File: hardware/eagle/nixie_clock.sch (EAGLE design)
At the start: 62 parts, among them IC1 74141N, IC10 7477N, IC11 74141N, IC12 7477N, IC13 74AC11238, IC2 7477N, IC3 74141N, IC4 7477N, IC5 74141N, IC6 7477N, IC7 74141N, IC8 7477N, IC9 74141N, J1_180V 22-27-2021-02, J1_5V1 22-27-2021-02, J1_5V2 22-27-2021-02

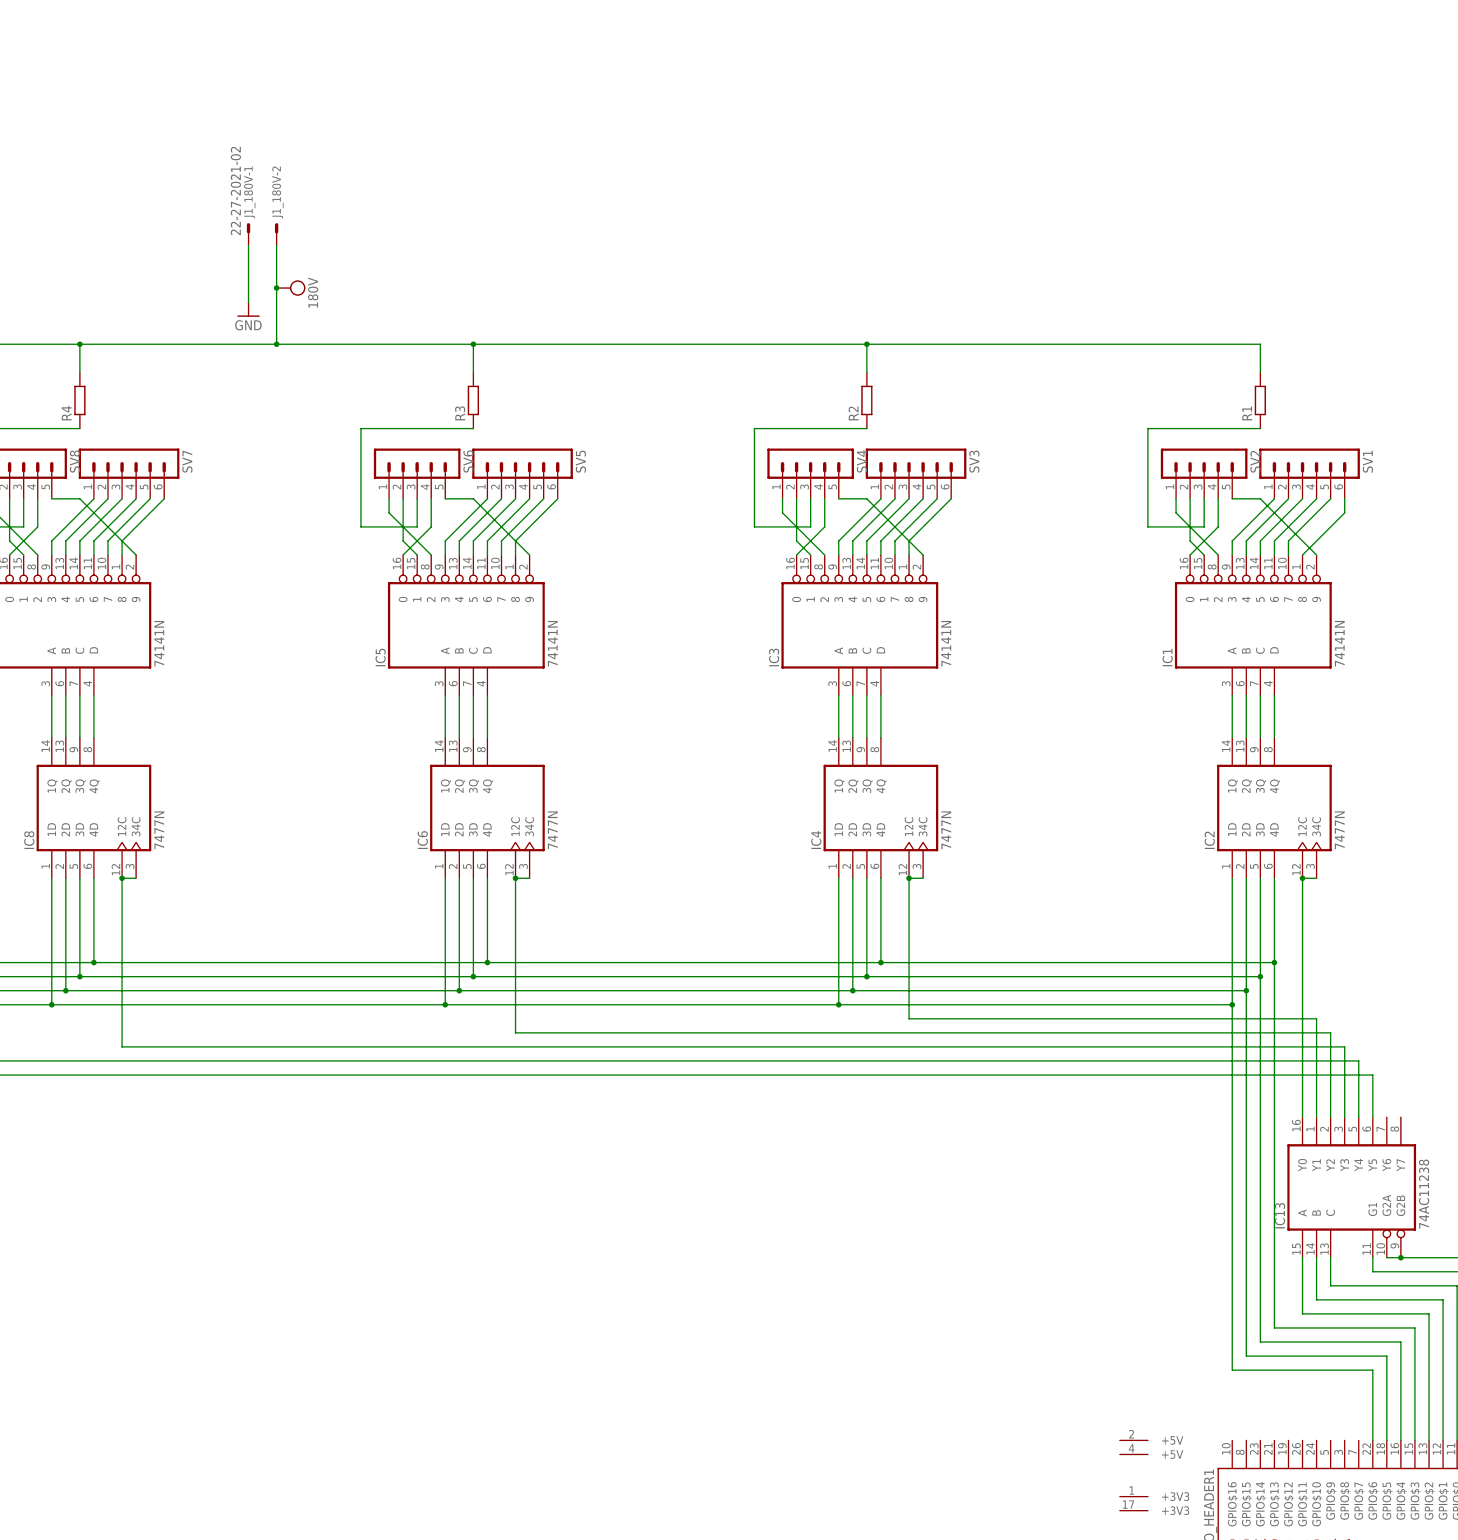
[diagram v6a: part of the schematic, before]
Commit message: Added relay
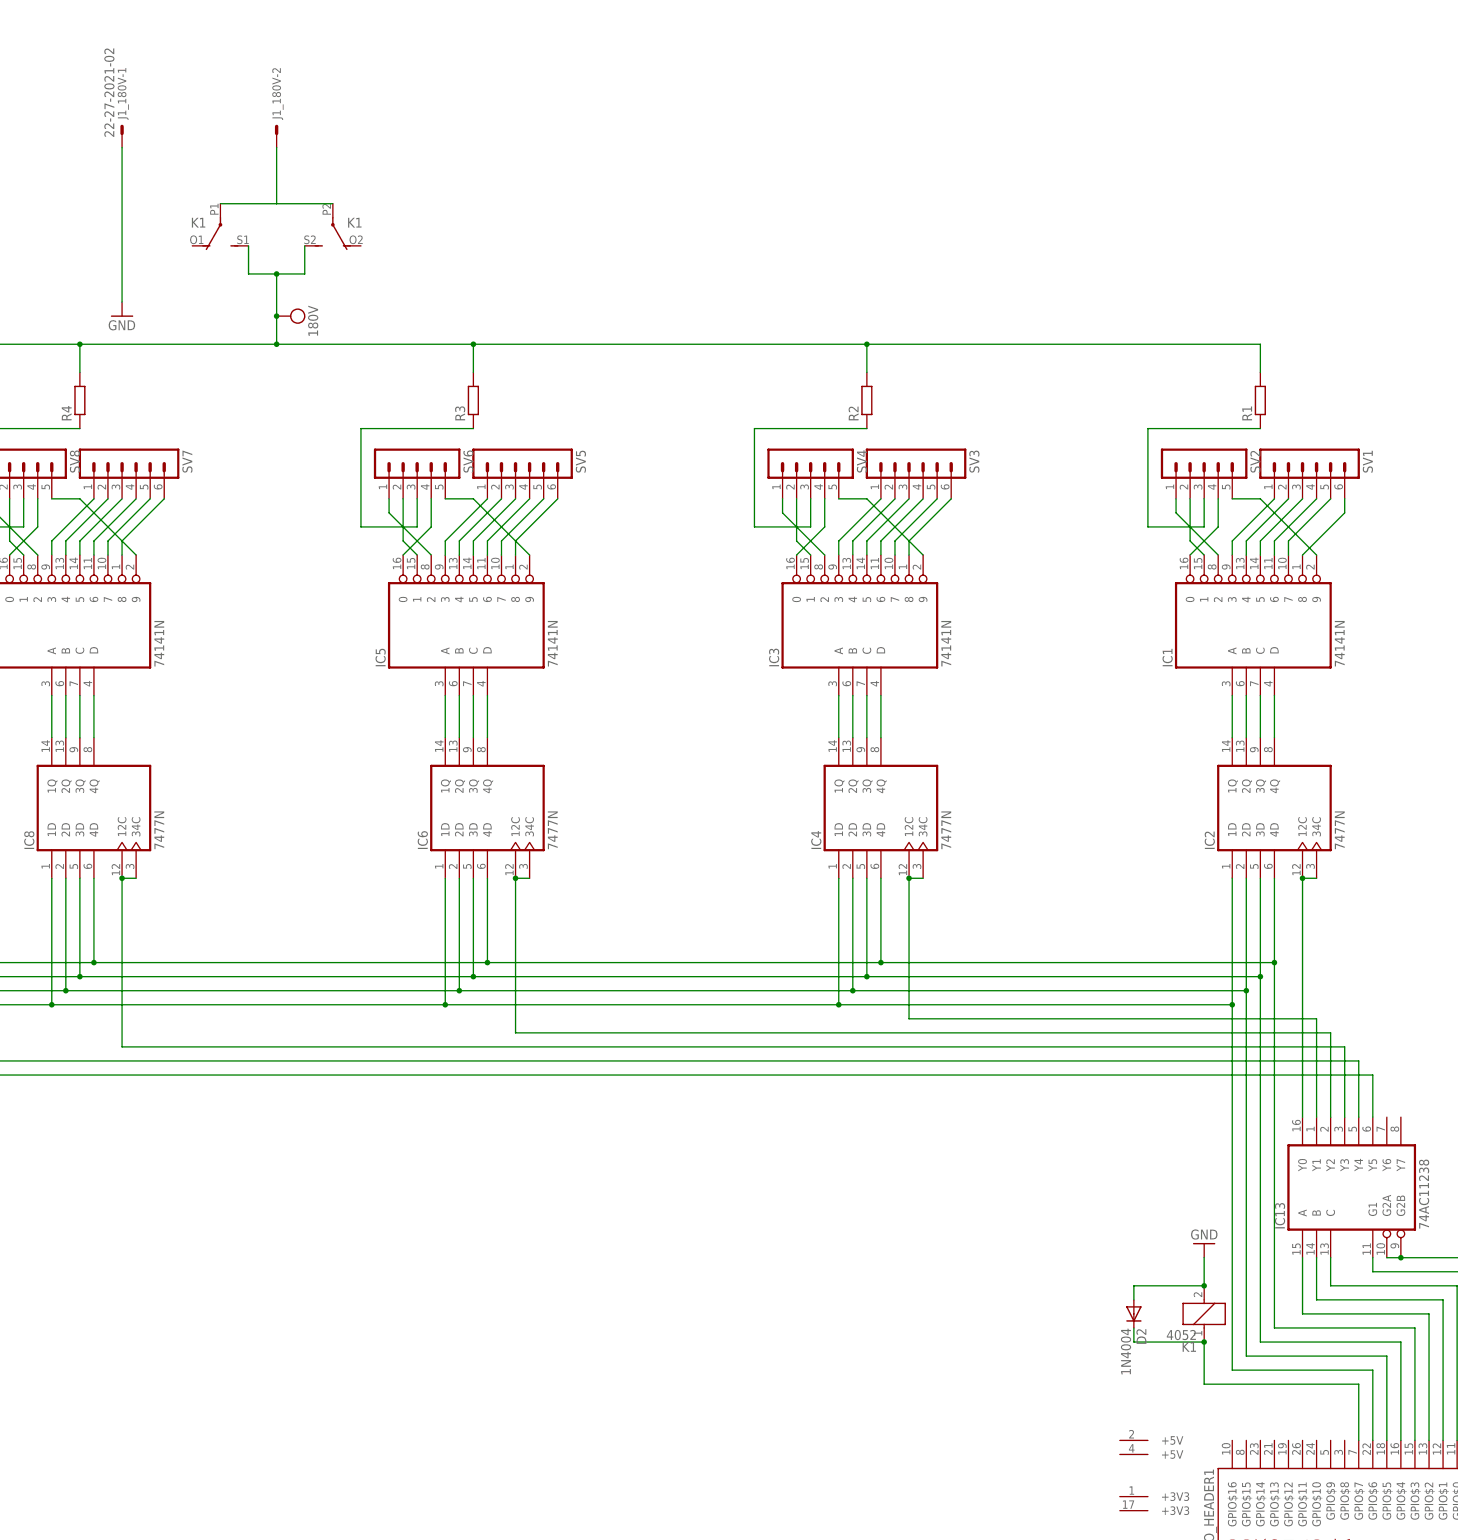
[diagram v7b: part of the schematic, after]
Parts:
- added D2: 1N4004, diode:1N4004
- added K1: 4052, relay:4052
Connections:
- new net N$126: J1_180V-2.S, K12.P, K13.P
- new net N$129: D2.C, GPIO_HEADER1G$1.GPIO$7, K11.1
- net GND: now also D2.A, K11.2
- net VCC: now also K12.S, K13.S; no longer J1_180V-2.S
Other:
- moved on the sheet: J1_180V-1, J1_180V-2
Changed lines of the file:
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@@
 <part name="J1_5V2" library="con-molex" deviceset="22-?-02" device="27-2021"/>
 <part name="D1" library="SparkFun-LED" deviceset="LED-RGB-CC-THRU" device="CLEAR"/>
+<part name="K1" library="relay" deviceset="4052" device=""/>
+<part name="D2" library="diode" deviceset="1N4004" device=""/>
+<part name="GND4" library="supply1" deviceset="GND" device=""/>
 </parts>
 <sheets>
@@
 <attribute name="MPN" x="530.86" y="287.02" size="1.778" layer="96" display="off"/>
 </instance>
-<instance part="SUPPLY1" gate="G$1" x="266.7" y="297.18" rot="R270"/>
+<instance part="SUPPLY1" gate="G$1" x="266.7" y="292.1" rot="R270"/>
 <instance part="IC3" gate="A" x="368.3" y="236.22" rot="R90">
 <attribute name="OC_FARNELL" x="368.3" y="236.22" size="1.778" layer="96" display="off"/>
@@
 <instance part="GND1" gate="1" x="492.76" y="111.76"/>
 <instance part="GPIO_HEADER1" gate="G$2" x="416.56" y="78.74"/>
-<instance part="J1_180V" gate="-1" x="259.08" y="307.34" rot="R90"/>
-<instance part="J1_180V" gate="-2" x="264.16" y="307.34" rot="R90"/>
+<instance part="J1_180V" gate="-1" x="236.22" y="325.12" rot="R90"/>
+<instance part="J1_180V" gate="-2" x="264.16" y="325.12" rot="R90"/>
 <instance part="J1_5V1" gate="-1" x="241.3" y="25.4" rot="R270"/>
 <instance part="J1_5V1" gate="-2" x="241.3" y="45.72" rot="R90"/>
-<instance part="GND2" gate="1" x="259.08" y="292.1"/>
+<instance part="GND2" gate="1" x="236.22" y="292.1"/>
 <instance part="GND3" gate="1" x="502.92" y="17.78"/>
 <instance part="SV13" gate="1" x="530.86" y="246.38" rot="MR90"/>
@@
 <instance part="J1_5V2" gate="-2" x="213.36" y="45.72" rot="R90"/>
 <instance part="D1" gate="G$1" x="561.34" y="281.94" rot="R90"/>
+<instance part="K1" gate="1" x="431.8" y="111.76" rot="R180"/>
+<instance part="K1" gate="2" x="254" y="309.88" rot="R180"/>
+<instance part="K1" gate="3" x="274.32" y="309.88" rot="MR180"/>
+<instance part="D2" gate="1" x="419.1" y="111.76" rot="R270"/>
+<instance part="GND4" gate="1" x="431.8" y="124.46" rot="R180"/>
 </instances>
 <busses>
@@
 </segment>
 </net>
-<net name="VCC" class="1">
-<segment>
-<pinref part="R6" gate="G$1" pin="2"/>
-<wire x1="86.36" y1="281.94" x2="86.36" y2="287.02" width="1.27" layer="91"/>
-<wire x1="86.36" y1="287.02" x2="157.48" y2="287.02" width="1.27" layer="91"/>
-<pinref part="SUPPLY1" gate="G$1" pin="VCC"/>
-<wire x1="157.48" y1="287.02" x2="228.6" y2="287.02" width="1.27" layer="91"/>
-<wire x1="228.6" y1="287.02" x2="264.16" y2="287.02" width="1.27" layer="91"/>
-<wire x1="264.16" y1="287.02" x2="299.72" y2="287.02" width="1.27" layer="91"/>
-<wire x1="299.72" y1="287.02" x2="370.84" y2="287.02" width="1.27" layer="91"/>
-<wire x1="370.84" y1="287.02" x2="441.96" y2="287.02" width="1.27" layer="91"/>
-<wire x1="264.16" y1="297.18" x2="264.16" y2="287.02" width="1.27" layer="91"/>
-<junction x="264.16" y="287.02"/>
-<pinref part="R3" gate="G$1" pin="2"/>
-<wire x1="299.72" y1="281.94" x2="299.72" y2="287.02" width="1.27" layer="91"/>
-<junction x="299.72" y="287.02"/>
-<pinref part="R2" gate="G$1" pin="2"/>
-<wire x1="370.84" y1="281.94" x2="370.84" y2="287.02" width="1.27" layer="91"/>
-<junction x="370.84" y="287.02"/>
-<pinref part="R4" gate="G$1" pin="2"/>
-<wire x1="228.6" y1="281.94" x2="228.6" y2="287.02" width="1.27" layer="91"/>
-<junction x="228.6" y="287.02"/>
-<pinref part="R5" gate="G$1" pin="2"/>
-<wire x1="157.48" y1="281.94" x2="157.48" y2="287.02" width="1.27" layer="91"/>
-<junction x="157.48" y="287.02"/>
-<pinref part="J1_180V" gate="-2" pin="S"/>
-<wire x1="264.16" y1="304.8" x2="264.16" y2="297.18" width="1.27" layer="91"/>
-<junction x="264.16" y="297.18"/>
-<pinref part="R1" gate="G$1" pin="2"/>
-<wire x1="441.96" y1="287.02" x2="441.96" y2="281.94" width="1.27" layer="91"/>
-</segment>
-</net>
 <net name="N$97" class="0">
 <segment>
@@
 <pinref part="J1_180V" gate="-1" pin="S"/>
 <pinref part="GND2" gate="1" pin="GND"/>
-<wire x1="259.08" y1="304.8" x2="259.08" y2="294.64" width="1.27" layer="91"/>
+<wire x1="236.22" y1="322.58" x2="236.22" y2="294.64" width="1.27" layer="91"/>
 </segment>
 <segment>
@@
 <pinref part="IC1" gate="P" pin="GND"/>
 <junction x="259.08" y="27.94"/>
+</segment>
+<segment>
+<pinref part="D2" gate="1" pin="A"/>
+<pinref part="K1" gate="1" pin="2"/>
+<wire x1="419.1" y1="114.3" x2="419.1" y2="116.84" width="0.1524" layer="91"/>
+<wire x1="419.1" y1="116.84" x2="431.8" y2="116.84" width="0.1524" layer="91"/>
+<pinref part="GND4" gate="1" pin="GND"/>
+<wire x1="431.8" y1="116.84" x2="431.8" y2="121.92" width="0.1524" layer="91"/>
+<junction x="431.8" y="116.84"/>
 </segment>
 </net>
@@
 </segment>
 </net>
+<net name="N$126" class="1">
+<segment>
+<pinref part="J1_180V" gate="-2" pin="S"/>
+<pinref part="K1" gate="2" pin="P"/>
+<wire x1="264.16" y1="312.42" x2="254" y2="312.42" width="1.27" layer="91"/>
+<pinref part="K1" gate="3" pin="P"/>
+<wire x1="264.16" y1="322.58" x2="264.16" y2="312.42" width="1.27" layer="91"/>
+<wire x1="264.16" y1="312.42" x2="274.32" y2="312.42" width="1.27" layer="91"/>
+</segment>
+</net>
+<net name="VCC" class="1">
+<segment>
+<pinref part="K1" gate="2" pin="S"/>
+<wire x1="259.08" y1="304.8" x2="259.08" y2="299.72" width="1.27" layer="91"/>
+<wire x1="259.08" y1="299.72" x2="264.16" y2="299.72" width="1.27" layer="91"/>
+<pinref part="SUPPLY1" gate="G$1" pin="VCC"/>
+<wire x1="264.16" y1="299.72" x2="264.16" y2="292.1" width="1.27" layer="91"/>
+<pinref part="R6" gate="G$1" pin="2"/>
+<wire x1="86.36" y1="281.94" x2="86.36" y2="287.02" width="1.27" layer="91"/>
+<wire x1="86.36" y1="287.02" x2="157.48" y2="287.02" width="1.27" layer="91"/>
+<wire x1="157.48" y1="287.02" x2="228.6" y2="287.02" width="1.27" layer="91"/>
+<wire x1="228.6" y1="287.02" x2="264.16" y2="287.02" width="1.27" layer="91"/>
+<wire x1="264.16" y1="287.02" x2="299.72" y2="287.02" width="1.27" layer="91"/>
+<wire x1="299.72" y1="287.02" x2="370.84" y2="287.02" width="1.27" layer="91"/>
+<wire x1="370.84" y1="287.02" x2="441.96" y2="287.02" width="1.27" layer="91"/>
+<pinref part="R3" gate="G$1" pin="2"/>
+<wire x1="299.72" y1="281.94" x2="299.72" y2="287.02" width="1.27" layer="91"/>
+<junction x="299.72" y="287.02"/>
+<pinref part="R2" gate="G$1" pin="2"/>
+<wire x1="370.84" y1="281.94" x2="370.84" y2="287.02" width="1.27" layer="91"/>
+<junction x="370.84" y="287.02"/>
+<pinref part="R4" gate="G$1" pin="2"/>
+<wire x1="228.6" y1="281.94" x2="228.6" y2="287.02" width="1.27" layer="91"/>
+<junction x="228.6" y="287.02"/>
+<pinref part="R5" gate="G$1" pin="2"/>
+<wire x1="157.48" y1="281.94" x2="157.48" y2="287.02" width="1.27" layer="91"/>
+<junction x="157.48" y="287.02"/>
+<pinref part="R1" gate="G$1" pin="2"/>
+<wire x1="441.96" y1="287.02" x2="441.96" y2="281.94" width="1.27" layer="91"/>
+<wire x1="264.16" y1="292.1" x2="264.16" y2="287.02" width="1.27" layer="91"/>
+<junction x="264.16" y="292.1"/>
+<junction x="264.16" y="287.02"/>
+<pinref part="K1" gate="3" pin="S"/>
+<wire x1="269.24" y1="304.8" x2="269.24" y2="299.72" width="1.27" layer="91"/>
+<wire x1="269.24" y1="299.72" x2="264.16" y2="299.72" width="1.27" layer="91"/>
+<junction x="264.16" y="299.72"/>
+</segment>
+</net>
+<net name="N$129" class="0">
+<segment>
+<pinref part="K1" gate="1" pin="1"/>
+<wire x1="431.8" y1="106.68" x2="431.8" y2="99.06" width="0.1524" layer="91"/>
+<wire x1="431.8" y1="99.06" x2="459.74" y2="99.06" width="0.1524" layer="91"/>
+<pinref part="GPIO_HEADER1" gate="G$1" pin="GPIO$7"/>
+<wire x1="459.74" y1="99.06" x2="459.74" y2="88.9" width="0.1524" layer="91"/>
+<pinref part="D2" gate="1" pin="C"/>
+<wire x1="431.8" y1="106.68" x2="419.1" y2="106.68" width="0.1524" layer="91"/>
+<wire x1="419.1" y1="106.68" x2="419.1" y2="109.22" width="0.1524" layer="91"/>
+<junction x="431.8" y="106.68"/>
+</segment>
+</net>

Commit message: Added rotary encoder example
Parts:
- removed D1: LED-RGB-CC-THRUCLEAR, SparkFun-LED:LED-RGB-CC-THRUCLEAR
- added SV15, SV16: (no value), con-lstb:MA05-1
- added SW1: ROTARTY_ENCODER, SparkFun-Electromechanical:ROTARTY_ENCODER
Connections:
- new net N$127: GPIO_HEADER1G$1.GPIO$12, SV16.4
- new net N$128: SV15.4, SW1.A
- new net N$130: GPIO_HEADER1G$1.GPIO$10
- new net N$131: SV15.3, SW1.SW-
- new net N$132: SV15.1, SW1.SW+
- new net N$133: SV15.2, SW1.C
- new net N$134: SV15.5, SW1.B
- new net N$135: GPIO_HEADER1G$1.GPIO$11, SV16.5
- new net N$136: GPIO_HEADER1G$1.GPIO$13, SV16.3
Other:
- moved on the sheet: B1, C1, C10, C11, C12, C13, C14, C15, C2, C3, C4, C5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
